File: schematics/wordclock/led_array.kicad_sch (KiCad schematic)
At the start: 67 parts, among them U2 MAX7219

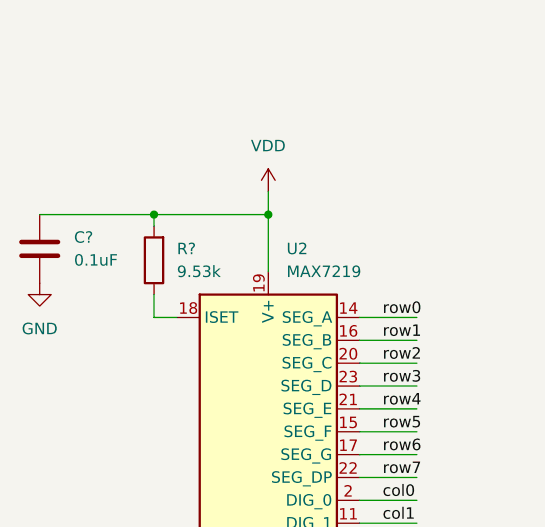
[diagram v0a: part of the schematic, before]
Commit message: Finish defining words, schematic updates
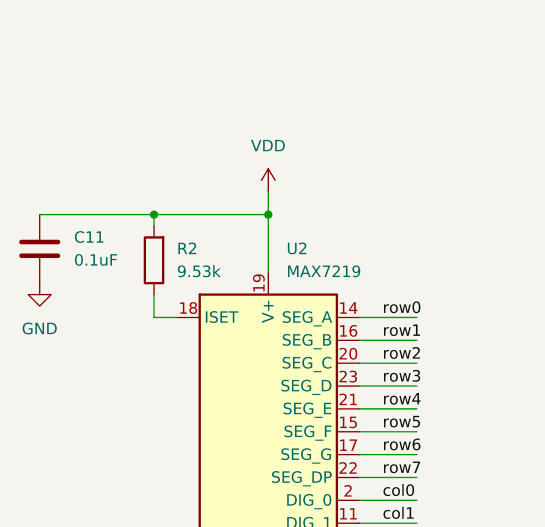
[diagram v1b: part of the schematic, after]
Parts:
- C11: renamed from C?; footprint (none) -> Capacitor_SMD:C_0805_2012Metric
- R2: renamed from R?; footprint (none) -> Resistor_SMD:R_0805_2012Metric
